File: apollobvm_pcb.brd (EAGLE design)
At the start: 98 x 60 mm, 25 parts

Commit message: Fixed some final issues with initial board
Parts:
- moved C6 3.00 mm to (58.0, 23.0)
- moved C7 3.00 mm to (55.0, 23.0), turned to 270 degrees
- turned C1 to 270 degrees
- turned C2 to 270 degrees
- turned C3 to 270 degrees
- turned C4 to 270 degrees
- turned C5 to 270 degrees
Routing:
- net N$14: track 105.8 -> 148.6 mm, vias 1 -> 0
- net N$9: track 75.0 -> 56.0 mm, vias 0 -> 1
- net +5V: track 203.1 -> 221.4 mm, vias 4 -> 3
- net N$24: track 76.7 -> 59.0 mm
- net N$4: track 52.2 -> 65.6 mm, vias 1 -> 0
- net N$1: track 88.1 -> 100.8 mm
- net N$15: track 42.1 -> 54.7 mm, vias 1 -> 0
- net N$17: track 43.0 -> 30.7 mm, vias 0 -> 1
- net N$3: track 65.3 -> 53.5 mm
- net N$20: track 66.0 -> 77.1 mm, vias 0 -> 1
- net N$7: track 46.8 -> 39.0 mm, vias 0 -> 1
- net N$25: track 55.3 -> 62.1 mm
- net GND: track 197.0 -> 190.5 mm, vias 1 -> 2
- net N$19: track 72.6 -> 66.5 mm
- net VCC: track 115.7 -> 120.9 mm, vias 0 -> 2
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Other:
- board text added: "ApolloBVM V1.0"

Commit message: Moved PWM leads apart for servos
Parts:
- moved SER_1 3.00 mm to (23.0, 48.0)
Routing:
- net VCC: track 120.9 -> 123.9 mm
- net GND: track 190.5 -> 193.5 mm
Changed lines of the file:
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@@
 <attribute name="VALUE" x="91.08" y="34.65" size="1.016" layer="27" ratio="10" rot="R90"/>
 </element>
-<element name="SER_1" library="con-molex" library_urn="urn:adsk.eagle:library:165" package="22-23-2031" package3d_urn="urn:adsk.eagle:package:8078634/1" value="22-23-2031" x="20" y="48" smashed="yes" rot="R90">
-<attribute name="MF" value="MOLEX" x="20" y="48" size="1.778" layer="27" rot="R90" display="off"/>
-<attribute name="MPN" value="22-23-2031" x="20" y="48" size="1.778" layer="27" rot="R90" display="off"/>
-<attribute name="NAME" x="16.19" y="44.19" size="1.016" layer="25" ratio="10" rot="R90"/>
-<attribute name="OC_FARNELL" value="1462950" x="20" y="48" size="1.778" layer="27" rot="R90" display="off"/>
-<attribute name="OC_NEWARK" value="30C0862" x="20" y="48" size="1.778" layer="27" rot="R90" display="off"/>
-<attribute name="POPULARITY" value="35" x="20" y="48" size="1.778" layer="27" rot="R90" display="off"/>
-<attribute name="VALUE" x="25.08" y="44.19" size="1.016" layer="27" ratio="10" rot="R90"/>
+<element name="SER_1" library="con-molex" library_urn="urn:adsk.eagle:library:165" package="22-23-2031" package3d_urn="urn:adsk.eagle:package:8078634/1" value="22-23-2031" x="23" y="48" smashed="yes" rot="R90">
+<attribute name="MF" value="MOLEX" x="23" y="48" size="1.778" layer="27" rot="R90" display="off"/>
+<attribute name="MPN" value="22-23-2031" x="23" y="48" size="1.778" layer="27" rot="R90" display="off"/>
+<attribute name="NAME" x="19.19" y="44.19" size="1.016" layer="25" ratio="10" rot="R90"/>
+<attribute name="OC_FARNELL" value="1462950" x="23" y="48" size="1.778" layer="27" rot="R90" display="off"/>
+<attribute name="OC_NEWARK" value="30C0862" x="23" y="48" size="1.778" layer="27" rot="R90" display="off"/>
+<attribute name="POPULARITY" value="35" x="23" y="48" size="1.778" layer="27" rot="R90" display="off"/>
+<attribute name="VALUE" x="28.08" y="44.19" size="1.016" layer="27" ratio="10" rot="R90"/>
 </element>
 <element name="SER_2" library="con-molex" library_urn="urn:adsk.eagle:library:165" package="22-23-2031" package3d_urn="urn:adsk.eagle:package:8078634/1" value="22-23-2031" x="11" y="48" smashed="yes" rot="R90">
@@
 <wire x1="58" y1="22" x2="58" y2="22.15" width="0.4064" layer="1"/>
 <wire x1="55" y1="22" x2="55" y2="22.15" width="0.4064" layer="1"/>
-<wire x1="20" y1="45.5" x2="11" y2="45.5" width="0.4064" layer="1"/>
+<wire x1="23" y1="45.5" x2="11" y2="45.5" width="0.4064" layer="1"/>
 <wire x1="11" y1="45.5" x2="11" y2="45.46" width="0.4064" layer="1"/>
-<wire x1="20" y1="45.5" x2="20" y2="45.46" width="0.4064" layer="1"/>
+<wire x1="23" y1="45.5" x2="23" y2="45.46" width="0.4064" layer="1"/>
 <wire x1="11" y1="13" x2="25" y2="13" width="0.4064" layer="1"/>
 <wire x1="25" y1="13" x2="25.4" y2="13.05" width="0.4064" layer="1"/>
@@
 <contactref element="SER_1" pad="2"/>
 <contactref element="PWR_IN" pad="2"/>
-<wire x1="20" y1="48" x2="11" y2="48" width="0.4064" layer="1"/>
+<wire x1="23" y1="48" x2="11" y2="48" width="0.4064" layer="1"/>
 <wire x1="60" y1="23.5" x2="58" y2="23.5" width="0.4064" layer="1"/>
 <wire x1="60" y1="23.5" x2="60.5" y2="23" width="0.4064" layer="16"/>
@@
 <wire x1="36.5" y1="37" x2="36.5" y2="33" width="0.4064" layer="16"/>
 <wire x1="23" y1="50.5" x2="36.5" y2="37" width="0.4064" layer="1"/>
-<wire x1="20" y1="50.5" x2="23" y2="50.5" width="0.4064" layer="1"/>
 <wire x1="39" y1="30.5" x2="39.24" y2="30.41" width="0.4064" layer="16"/>
-<wire x1="20" y1="50.5" x2="11" y2="50.5" width="0.4064" layer="1"/>
+<wire x1="23" y1="50.5" x2="11" y2="50.5" width="0.4064" layer="1"/>
 <wire x1="11" y1="50.5" x2="11" y2="50.54" width="0.4064" layer="1"/>
-<wire x1="20" y1="50.5" x2="20" y2="50.54" width="0.4064" layer="1"/>
+<wire x1="23" y1="50.5" x2="23" y2="50.54" width="0.4064" layer="1"/>
 <via x="36.5" y="37" extent="1-16" drill="0.7874"/>
 </signal>

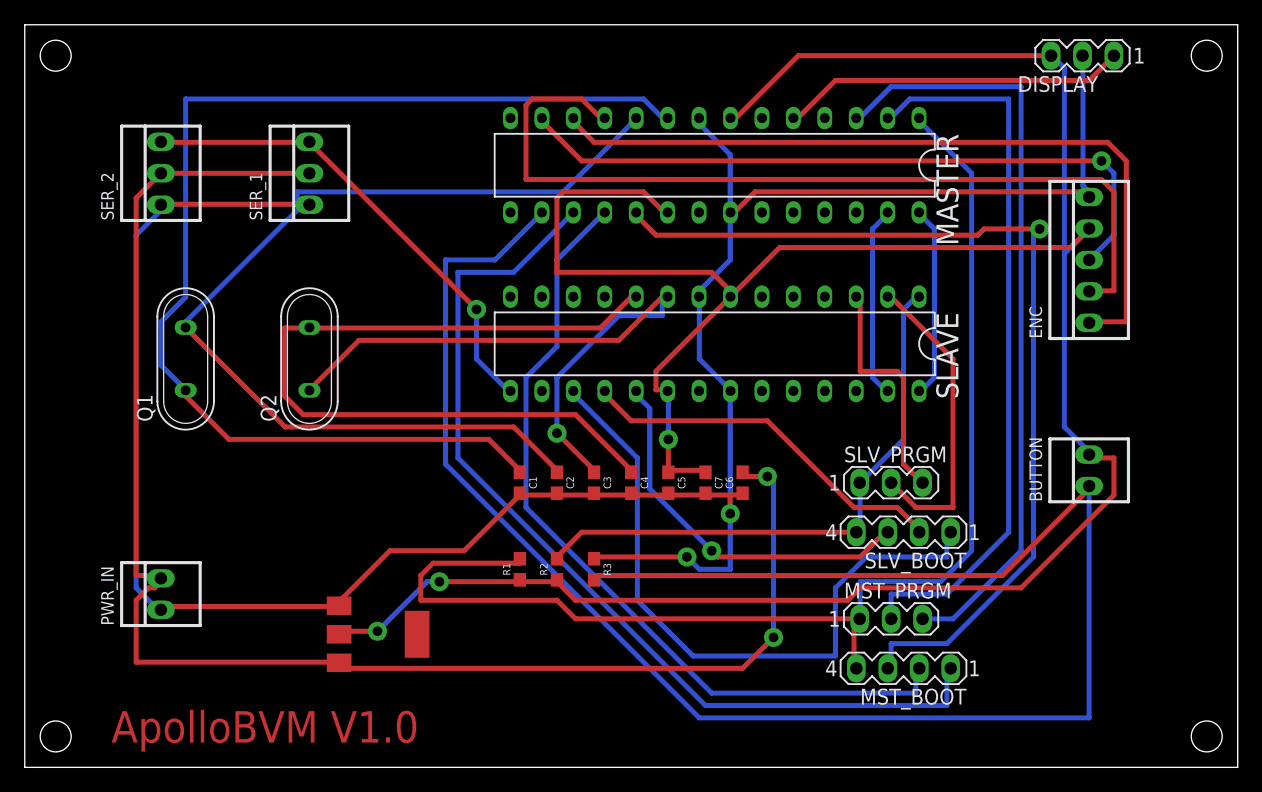
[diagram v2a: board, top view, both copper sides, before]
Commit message: Added millable version
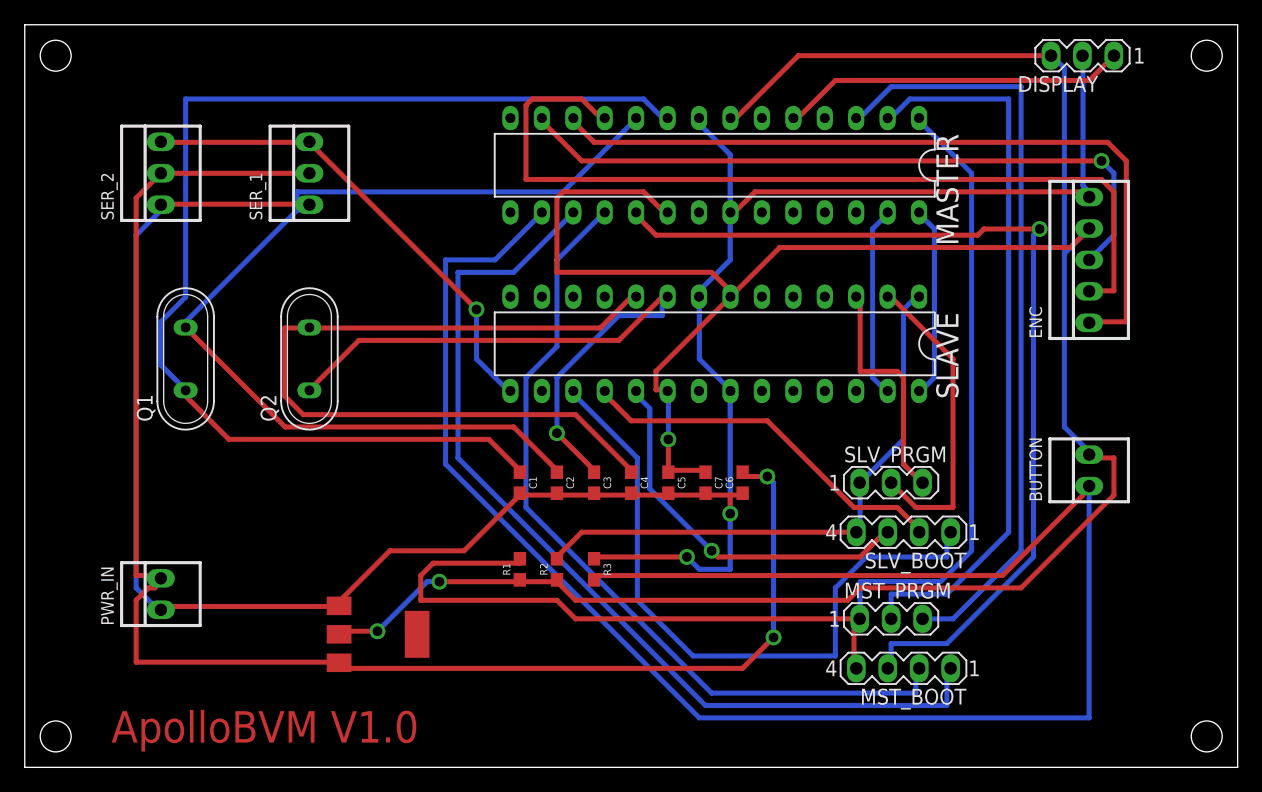
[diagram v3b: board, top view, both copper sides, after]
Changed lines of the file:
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@@
 <drawing>
 <settings>
-<setting alwaysvectorfont="no"/>
+<setting alwaysvectorfont="yes"/>
 <setting verticaltext="up"/>
 </settings>
@@
 </class>
 </classes>
-<designrules name="OthermillDRC_1_64_v2">
-<description language="en">&lt;b&gt;Othermill EAGLE Design Rules v2&lt;/b&gt;&lt;p&gt;DRC for Othermill, 1/64&quot; tool&lt;/p&gt;&lt;b&gt;-- Rules --&lt;/b&gt;&lt;li&gt;8 mil traces&lt;/li&gt;&lt;li&gt;15.7mil clearance&lt;/li&gt;</description>
+<designrules name="OthermillDRC_1_32_v2">
+<description language="en">&lt;b&gt;Othermill EAGLE Design Rules v2&lt;/b&gt;&lt;p&gt;DRC for Othermill, 1/32&quot; tool&lt;/p&gt;&lt;b&gt;-- Rules --&lt;/b&gt;&lt;li&gt;8 mil traces&lt;/li&gt;&lt;li&gt;31.26mil clearance&lt;/li&gt;</description>
 <param name="layerSetup" value="(1*16)"/>
 <param name="mtCopper" value="0.035mm 0.035mm 0.035mm 0.035mm 0.035mm 0.035mm 0.035mm 0.035mm 0.035mm 0.035mm 0.035mm 0.035mm 0.035mm 0.035mm 0.035mm 0.035mm"/>
 <param name="mtIsolate" value="1.5mm 0.15mm 0.2mm 0.15mm 0.2mm 0.15mm 0.2mm 0.15mm 0.2mm 0.15mm 0.2mm 0.15mm 0.2mm 0.15mm 0.2mm"/>
-<param name="mdWireWire" value="0.39878125mm"/>
-<param name="mdWirePad" value="0.39878125mm"/>
-<param name="mdWireVia" value="0.39878125mm"/>
-<param name="mdPadPad" value="0.39878125mm"/>
-<param name="mdPadVia" value="0.39878125mm"/>
-<param name="mdViaVia" value="0.39878125mm"/>
+<param name="mdWireWire" value="0.794003125mm"/>
+<param name="mdWirePad" value="0.794003125mm"/>
+<param name="mdWireVia" value="0.794003125mm"/>
+<param name="mdPadPad" value="0.794003125mm"/>
+<param name="mdPadVia" value="0.794003125mm"/>
+<param name="mdViaVia" value="0.794003125mm"/>
 <param name="mdSmdPad" value="0mil"/>
 <param name="mdSmdVia" value="0mil"/>
@@
 <param name="mdDrill" value="1mil"/>
 <param name="mdSmdStop" value="0mil"/>
-<param name="msWidth" value="16mil"/>
-<param name="msDrill" value="31mil"/>
+<param name="msWidth" value="8mil"/>
+<param name="msDrill" value="0.8mm"/>
 <param name="msMicroVia" value="9.99mm"/>
 <param name="msBlindViaRatio" value="0.5"/>
@@
 <param name="rvMicroViaOuter" value="0.25"/>
 <param name="rvMicroViaInner" value="0.25"/>
-<param name="rlMinPadTop" value="0mil"/>
-<param name="rlMaxPadTop" value="9999mil"/>
-<param name="rlMinPadInner" value="0mil"/>
-<param name="rlMaxPadInner" value="9999mil"/>
-<param name="rlMinPadBottom" value="0mil"/>
-<param name="rlMaxPadBottom" value="9999mil"/>
-<param name="rlMinViaOuter" value="15mil"/>
-<param name="rlMaxViaOuter" value="25mil"/>
+<param name="rlMinPadTop" value="10mil"/>
+<param name="rlMaxPadTop" value="20mil"/>
+<param name="rlMinPadInner" value="10mil"/>
+<param name="rlMaxPadInner" value="20mil"/>
+<param name="rlMinPadBottom" value="10mil"/>
+<param name="rlMaxPadBottom" value="20mil"/>
+<param name="rlMinViaOuter" value="10mil"/>
+<param name="rlMaxViaOuter" value="20mil"/>
 <param name="rlMinViaInner" value="8mil"/>
-<param name="rlMaxViaInner" value="25mil"/>
+<param name="rlMaxViaInner" value="20mil"/>
 <param name="rlMinMicroViaOuter" value="4mil"/>
 <param name="rlMaxMicroViaOuter" value="20mil"/>

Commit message: Made board for milling
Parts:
- moved SLV_BOOT 18.6 mm to (86.0, 8.00)
- moved SLV_PRGM 18.6 mm to (85.0, 12.0)
- moved R1 8.94 mm to (44.0, 8.00)
- moved R2 8.94 mm to (47.0, 8.00)
- moved R3 8.94 mm to (50.0, 8.00)
- moved C1 7.81 mm to (34.0, 18.0)
- moved C2 7.81 mm to (37.0, 18.0)
- moved C3 7.81 mm to (40.0, 18.0)
- moved C4 7.81 mm to (43.0, 18.0)
- moved C5 7.81 mm to (46.0, 18.0)
- moved C6 7.81 mm to (52.0, 18.0)
- moved C7 7.81 mm to (49.0, 18.0)
- moved ENC 4.12 mm to (90.0, 42.0)
- moved BUTTON 4.00 mm to (90.0, 24.0)
- moved MST_BOOT 4.00 mm to (67.0, 8.00)
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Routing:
- net N$12: track 62.3 -> 216.0 mm
- net +5V: track 221.4 -> 170.0 mm
- net N$14: track 148.6 -> 104.3 mm
- net N$23: track 19.2 -> 58.9 mm
- net N$2: track 46.6 -> 84.9 mm
- net GND: track 193.5 -> 230.8 mm, vias 2 -> 0
- net N$16: track 30.7 -> 62.4 mm
- net N$20: track 77.1 -> 47.5 mm
- net N$18: track 77.4 -> 49.9 mm
- net N$1: track 100.8 -> 73.6 mm, vias 0 -> 1
- net VCC: track 123.9 -> 98.8 mm, vias 2 -> 0
- net N$10: track 71.1 -> 50.9 mm
- net N$25: track 62.1 -> 43.5 mm, vias 0 -> 1
- net N$19: track 66.5 -> 49.5 mm, vias 0 -> 1
- net N$6: track 79.5 -> 96.3 mm, vias 0 -> 1
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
